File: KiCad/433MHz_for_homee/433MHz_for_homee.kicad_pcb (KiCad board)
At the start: 2 copper layers, 90 x 58.5 mm, 10 parts, among them Q1 BC547, Q2 BC547, U1 ESP32-C3_SUPERMINI_TH, U2 4x Level Converter Module (3.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

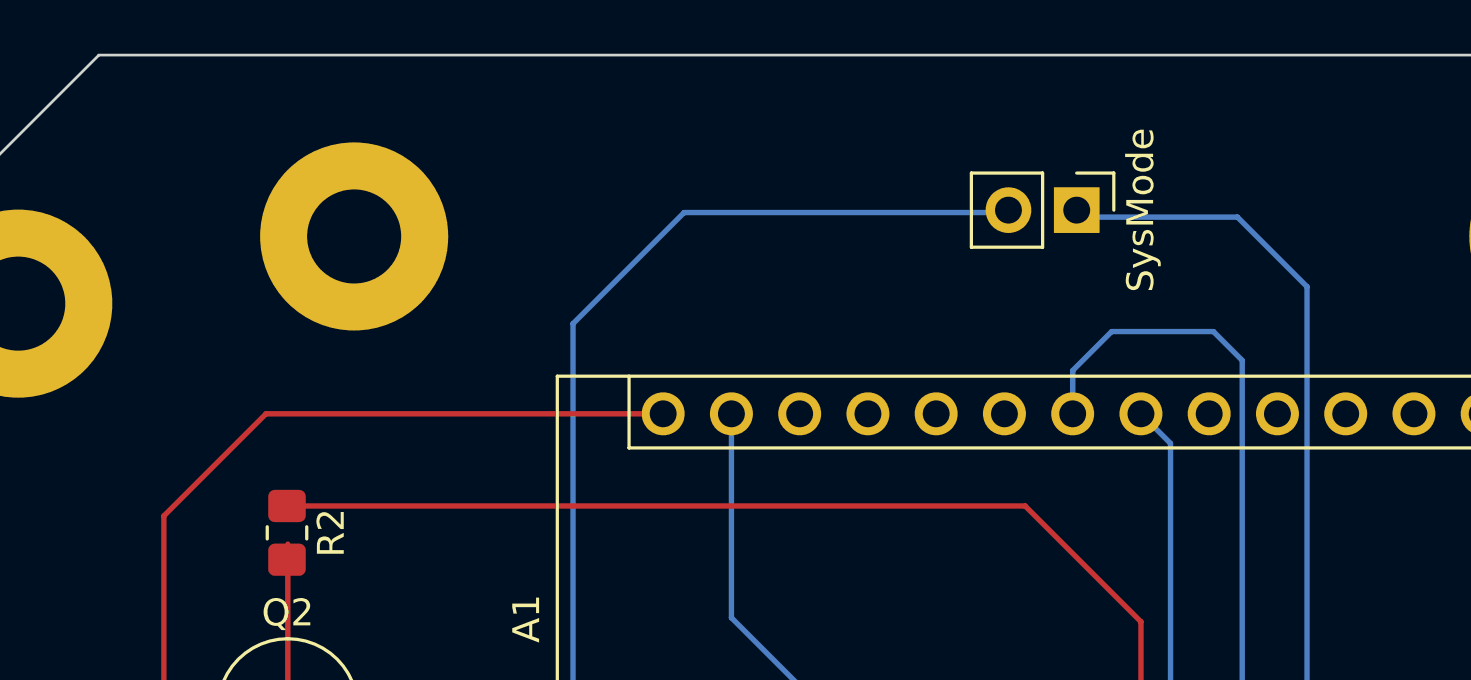
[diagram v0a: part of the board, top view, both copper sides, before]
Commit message: fixed a bug in the PCB
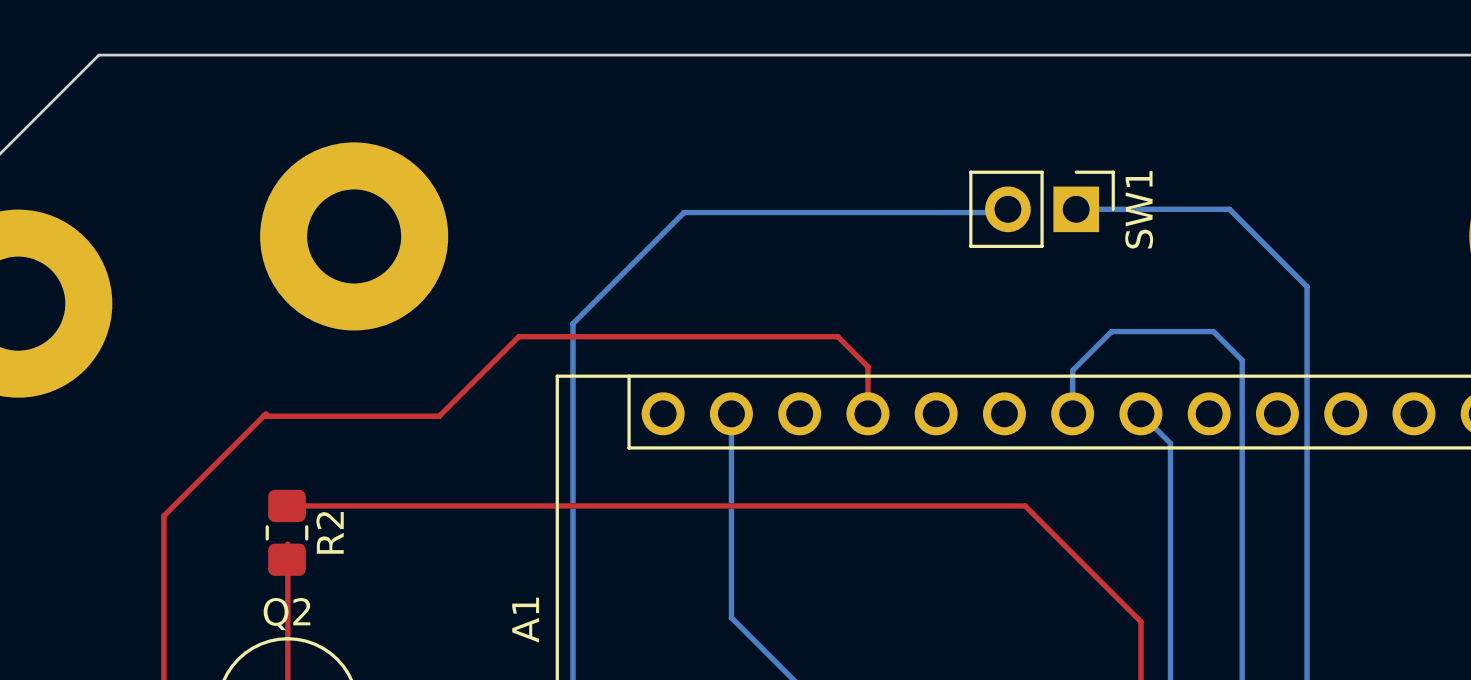
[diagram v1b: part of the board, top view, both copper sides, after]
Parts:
- removed SysMode: SysMode, Connector_PinHeader_2.54mm:PinHeader_1x02_P2.54mm_Vertical
- added SW1: SysMode, Connector_PinHeader_2.54mm:PinHeader_1x02_P2.54mm_Vertical, F.Cu at (96.7, 29.2)
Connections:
- A1 pad 27: unconnected-(A1-+5V-Pad27) -> +5V
- A1 pad 30: +5V -> unconnected-(A1-VIN-Pad30)
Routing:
- net +5V: track 124.2 -> 135.4 mm

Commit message: User manual updated
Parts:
- moved IC1 72.0 mm to (121.4, 113.4)
- moved U1 72.0 mm to (136.6, 120.9)
- moved A1 72.0 mm to (131.3, 103.8)
- moved Q1 72.0 mm to (170.3, 111.6)
- moved R1 72.0 mm to (170.5, 117.4)
- moved R2 72.0 mm to (117.3, 93.0)
- moved REF** 72.0 mm to (142.3, 104.5)
- moved SW1 72.0 mm to (146.7, 81.0)
- moved U2 72.0 mm to (157.7, 114.6)
- moved Q2 72.0 mm to (116.1, 99.5)
